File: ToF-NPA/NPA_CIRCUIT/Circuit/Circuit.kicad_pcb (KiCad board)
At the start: 2 copper layers, 110 x 94 mm, 11 parts, among them J1 BG302-02-A-L-G

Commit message: made coax easier to put in box
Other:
- board size 110 x 94 mm -> 110.5 x 90 mm
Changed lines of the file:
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@@
 		(tags "Connector")
 		(property "Reference" "J1"
-			(at 0 0 270)
+			(at 0 0 -90)
 			(layer "F.SilkS")
 			(hide yes)
@@
 		)
 		(property "Value" "BG302-02-A-L-G"
-			(at 0 0 270)
+			(at 0 0 -90)
 			(layer "F.SilkS")
 			(hide yes)
@@
 		)
 		(property "Value" "BG030-03-A-0450-0300-N-G"
-			(at 0 0 360)
+			(at 0 0 0)
 			(layer "F.SilkS")
 			(hide yes)
@@
 		(tags "Power Supply")
 		(property "Reference" "TBA 1-0521HI"
-			(at 7.35 1.65 270)
+			(at 7.35 1.65 -90)
 			(layer "F.SilkS")
 			(effects
@@
 		)
 		(property "Value" "TBA_1-0521HI"
-			(at 7.35 1.65 270)
+			(at 7.35 1.65 -90)
 			(layer "F.SilkS")
 			(hide yes)
@@
 		)
 		(fp_text user "${REFERENCE}"
-			(at 7.35 1.65 270)
+			(at 7.35 1.65 -90)
 			(layer "F.Fab")
 			(effects
@@
 		(tags "Integrated Circuit")
 		(property "Reference" "OpAmp"
-			(at 0 0 270)
+			(at 0 0 -90)
 			(layer "F.SilkS")
 			(effects
@@
 	)
 	(gr_line
-		(start 75 149)
-		(end 75 55)
+		(start 184.5 145)
+		(end 74.5 145)
 		(stroke
 			(width 0.05)
@@
 	)
 	(gr_line
-		(start 185 149)
-		(end 75 149)
+		(start 75 55)
+		(end 74.5 145)
 		(stroke
 			(width 0.05)
@@
 	(gr_line
 		(start 185 55)
-		(end 185 149)
+		(end 184.5 145)
 		(stroke
 			(width 0.05)
@@
 	)
 	(gr_circle
-		(center 180 145)
-		(end 183 145)
+		(center 180 140)
+		(end 183 140)
 		(stroke
 			(width 0.05)
@@
 	)
 	(gr_circle
-		(center 80 145)
-		(end 83 145)
+		(center 80 140)
+		(end 83 140)
 		(stroke
 			(width 0.05)

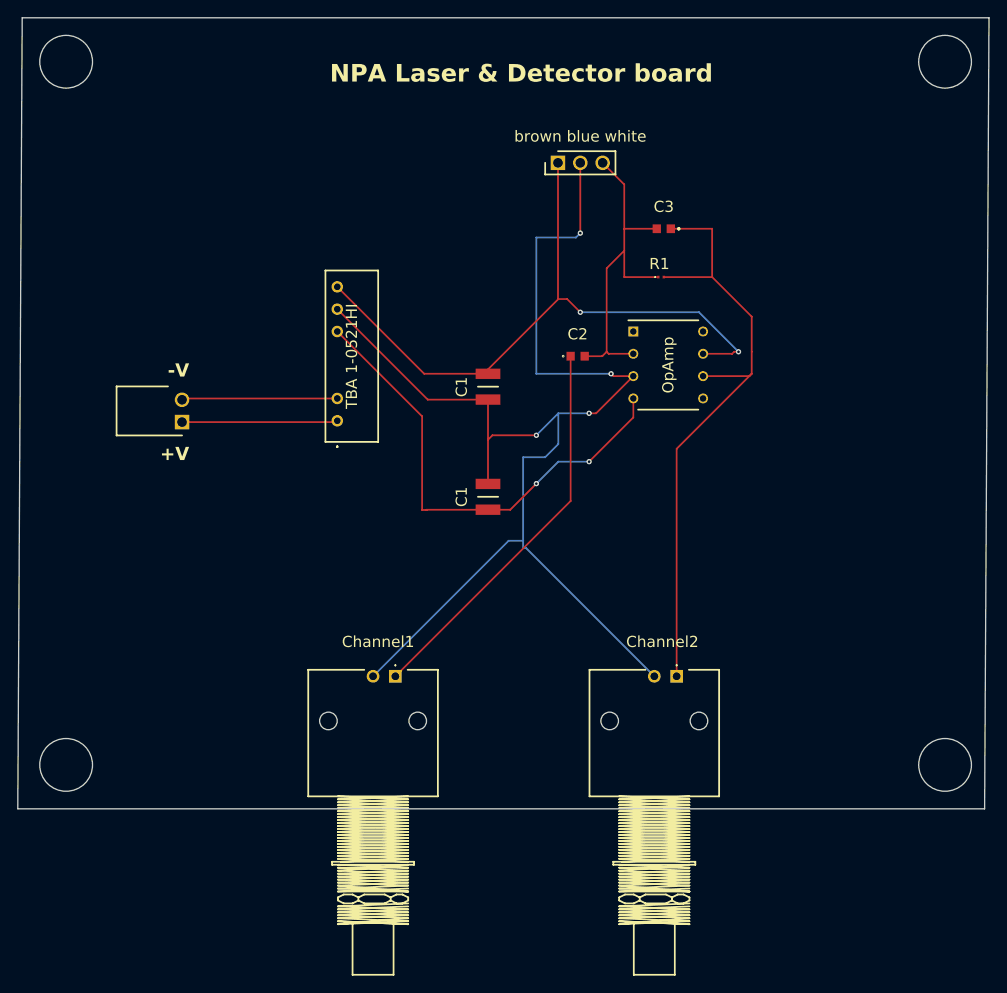
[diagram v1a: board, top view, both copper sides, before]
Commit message: changed resistor to 2W rating
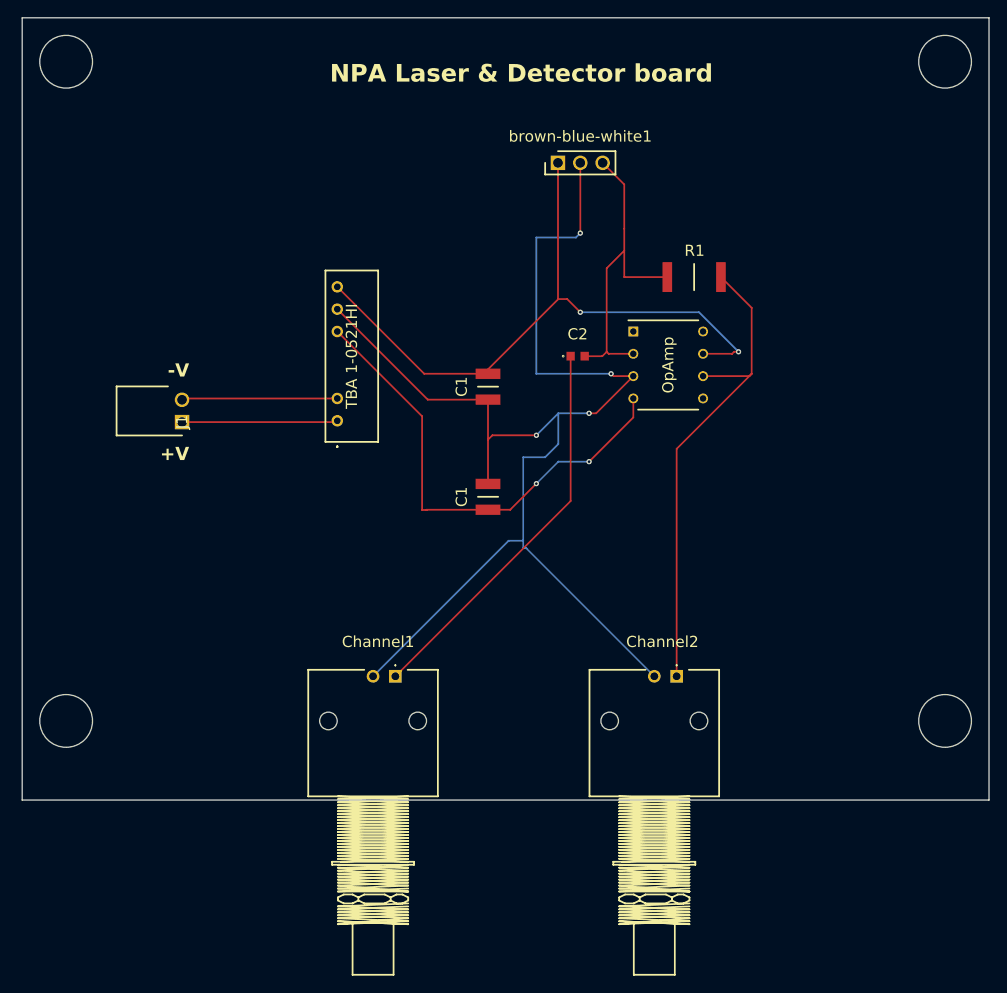
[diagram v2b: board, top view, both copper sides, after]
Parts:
- removed C3: CBR06C109B5GACAUTO, 1 pF KEMET:CBR06
- R1: value ERJ-1GJF1004C -> CRGP2512F1M0; footprint 1 MOhms R:ERJ1GJJ2R4C -> 1 MOhms R:RESC6432X65N
- brown-blue-white1: renamed from brown blue white
- moved R1 3.76 mm to (151.4, 84.5)
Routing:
- net Net-(OpAmp1-OUT): track 72.2 -> 56.0 mm
- net Net-(OpAmp1--IN): track 39.8 -> 37.1 mm
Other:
- board size 110.5 x 90 mm -> 110 x 89 mm

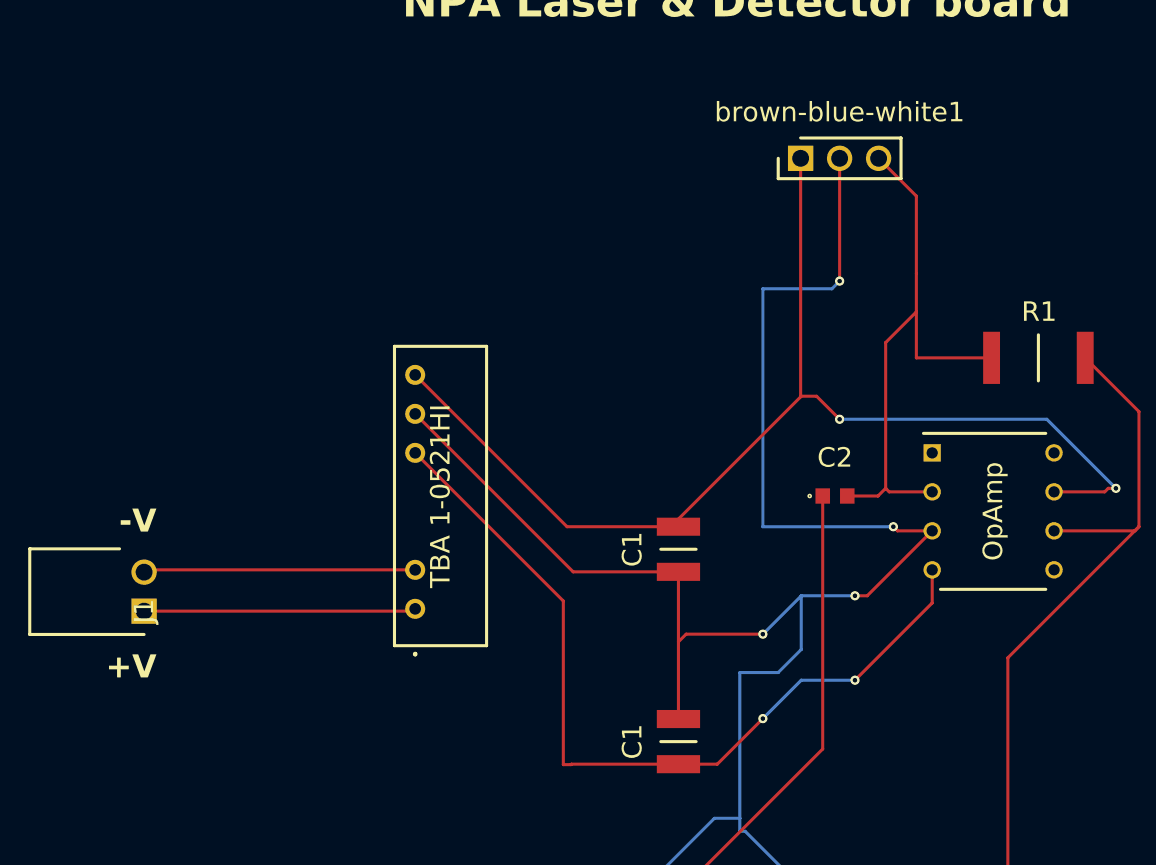
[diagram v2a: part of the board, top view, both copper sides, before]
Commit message: was wired wrong, happely catched it just in time
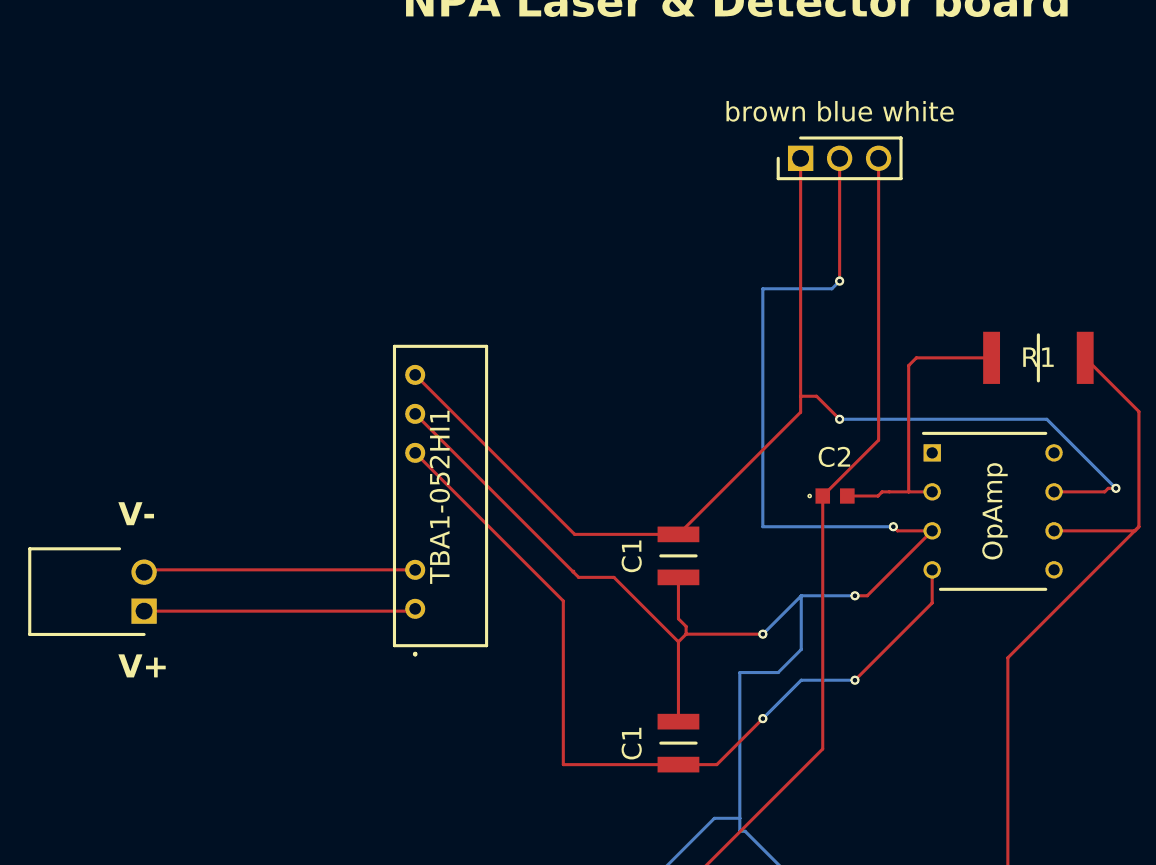
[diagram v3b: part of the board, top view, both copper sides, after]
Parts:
- removed the C1 at (128.0, 97.0)
- removed the C1 at (128.0, 109.5)
- added C1: 12103C106K4Z2A, 1C:CAPC3225X279N, F.Cu at (128.0, 97.4)
- added C1: 12103C106K4Z2A, 1C:CAPC3225X279N, F.Cu at (128.0, 109.6)
- TBA1-052HI1: renamed from TBA 1-0521HI
- brown blue white: renamed from brown-blue-white1
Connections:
- OpAmp pad 7: Net-(OpAmp1-V+) -> Net-(OpAmp1-+IN)
- TBA1-052HI1 pad 7: Net-(OpAmp1-V+) -> Net-(OpAmp1-+IN)
- brown blue white pad 1: Net-(OpAmp1-V+) -> Net-(OpAmp1-+IN)
- brown blue white pad 3: Net-(OpAmp1--IN) -> Net-(C2-Pad1)
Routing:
- net Net-(OpAmp1-+IN): track 153.3 -> 231.1 mm, vias 4 -> 6
- net Net-(OpAmp1-V+): track 75.7 -> 0.00 mm, vias 2 -> 0
- net Net-(C2-Pad1): track 44.7 -> 68.2 mm
- net Net-(OpAmp1--IN): track 37.1 -> 19.5 mm

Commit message: now we're done
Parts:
- removed the C1 at (128.0, 97.4)
- removed the C1 at (128.0, 109.6)
- removed OpAmp: LT1115CN8#PBF, LT1115CN8:DIP794W53P254L1016H394Q8N
- added C1: 12103C106K4Z2A, 1C:CAPC3225X279N, F.Cu at (128.0, 97.5)
- added C1: 12103C106K4Z2A, 1C:CAPC3225X279N, F.Cu at (128.0, 109.5)
- added OpAmp1: LT1115CN8#PBF, LT1115CN8:DIP794W53P254L1016H394Q8N, F.Cu at (148.5, 94.5)
- moved brown blue white 3.00 mm to (136.0, 68.5)
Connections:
- Channel1 pad 2: Net-(OpAmp1-+IN) -> GND
- Channel2 pad 2: Net-(OpAmp1-+IN) -> GND
- TBA1-052HI1 pad 5: Net-(OpAmp1-V-) -> -5V
- TBA1-052HI1 pad 6: Net-(OpAmp1-+IN) -> GND
- TBA1-052HI1 pad 7: Net-(OpAmp1-+IN) -> +5V
- brown blue white pad 1: Net-(OpAmp1-+IN) -> +5V
- brown blue white pad 2: Net-(OpAmp1-+IN) -> GND
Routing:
- net Net-(OpAmp1-+IN): track 231.1 -> 0.00 mm, vias 6 -> 0
- net GND: track 0.00 -> 146.2 mm, vias 0 -> 3
- net +5V: track 0.00 -> 79.5 mm, vias 0 -> 2
- net Net-(OpAmp1-V-): track 54.9 -> 0.00 mm, vias 2 -> 0
- net -5V: track 0.00 -> 54.6 mm, vias 0 -> 2
- net Net-(C2-Pad1): track 68.2 -> 71.2 mm

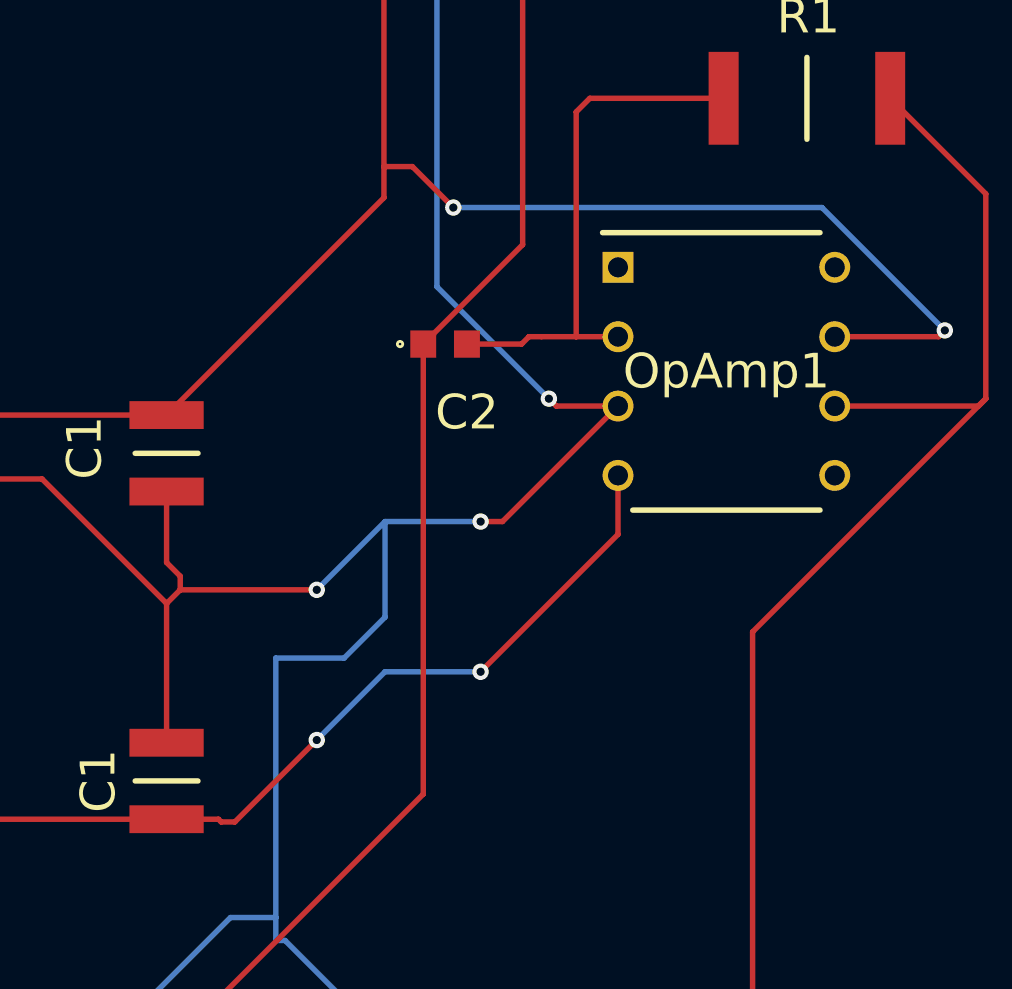
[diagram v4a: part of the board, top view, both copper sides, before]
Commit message: case now with step of circuit
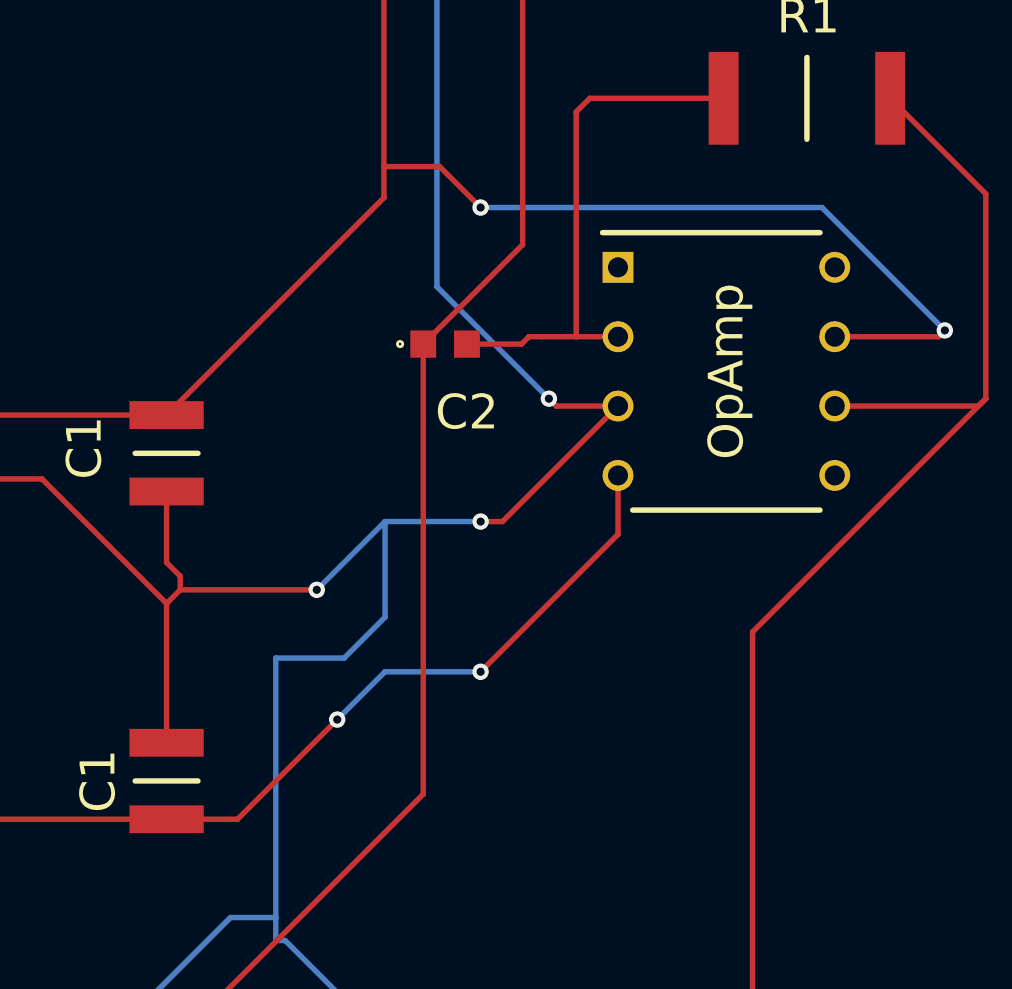
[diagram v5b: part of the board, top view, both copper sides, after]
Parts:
- renumbered OpAmp1 to OpAmp
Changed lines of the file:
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@@
 		(descr "N8 8-Lead PDIP")
 		(tags "Integrated Circuit")
-		(property "Reference" "OpAmp1"
-			(at 0 0 0)
+		(property "Reference" "OpAmp"
+			(at 0 0 -90)
 			(layer "F.SilkS")
 			(effects
@@
 	)
 	(segment
-		(start 137 87)
-		(end 135.96 87)
-		(width 0.2)
-		(layer "F.Cu")
-		(net 10)
-	)
-	(segment
 		(start 156.27 93.23)
 		(end 152.469 93.23)
@@
 	)
 	(segment
-		(start 138.5 88.5)
-		(end 137 87)
+		(start 156.5 93)
+		(end 156.27 93.23)
 		(width 0.2)
 		(layer "F.Cu")
@@
 	)
 	(segment
-		(start 156.5 93)
-		(end 156.27 93.23)
+		(start 135.96 68.5)
+		(end 135.96 87)
 		(width 0.2)
 		(layer "F.Cu")
@@
 	)
 	(segment
-		(start 135.96 68.5)
+		(start 138 87)
 		(end 135.96 87)
 		(width 0.2)
@@
 	)
 	(segment
+		(start 139.5 88.5)
+		(end 138 87)
+		(width 0.2)
+		(layer "F.Cu")
+		(net 10)
+	)
+	(segment
 		(start 135.96 87)
 		(end 135.96 88.14)
@@
 	)
 	(via
-		(at 138.5 88.5)
+		(at 139.5 88.5)
 		(size 0.6)
 		(drill 0.3)
@@
 	)
 	(segment
-		(start 138.5 88.5)
-		(end 152 88.5)
-		(width 0.2)
-		(layer "B.Cu")
-		(net 10)
-	)
-	(segment
 		(start 152 88.5)
 		(end 156.5 93)
@@
 	)
 	(segment
-		(start 129.9 110.9)
-		(end 128 110.9)
+		(start 139.5 88.5)
+		(end 152 88.5)
 		(width 0.2)
-		(layer "F.Cu")
-		(net 11)
+		(layer "B.Cu")
+		(net 10)
 	)
 	(segment
@@
 	)
 	(segment
-		(start 130.5 111)
-		(end 133.5 108)
+		(start 134.25 107.25)
+		(end 130.6 110.9)
 		(width 0.2)
 		(layer "F.Cu")
@@
 	)
 	(segment
-		(start 130 111)
-		(end 129.9 110.9)
+		(start 130.6 110.9)
+		(end 128 110.9)
 		(width 0.2)
 		(layer "F.Cu")
@@
 	)
 	(segment
-		(start 130.5 111)
-		(end 130 111)
-		(width 0.2)
-		(layer "F.Cu")
-		(net 11)
-	)
-	(segment
 		(start 144.531 98.31)
 		(end 144.531 100.469)
@@
 	)
 	(via
-		(at 133.5 108)
+		(at 134.25 107.25)
 		(size 0.6)
 		(drill 0.3)
@@
 	)
 	(segment
-		(start 133.5 108)
-		(end 136 105.5)
+		(start 136 105.5)
+		(end 139.5 105.5)
 		(width 0.2)
 		(layer "B.Cu")
@@
 	)
 	(segment
-		(start 136 105.5)
-		(end 139.5 105.5)
+		(start 134.25 107.25)
+		(end 136 105.5)
 		(width 0.2)
 		(layer "B.Cu")
